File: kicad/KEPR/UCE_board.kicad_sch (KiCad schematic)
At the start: 12 parts, among them IC1 ACS37041KLHBLT-010B3, IC2 ACS37041KLHBLT-010B3, IC3 ACS37041KLHBLT-010B3, U1 REF193, U2 STM32G484CETx, U3 AMS1117-3.3

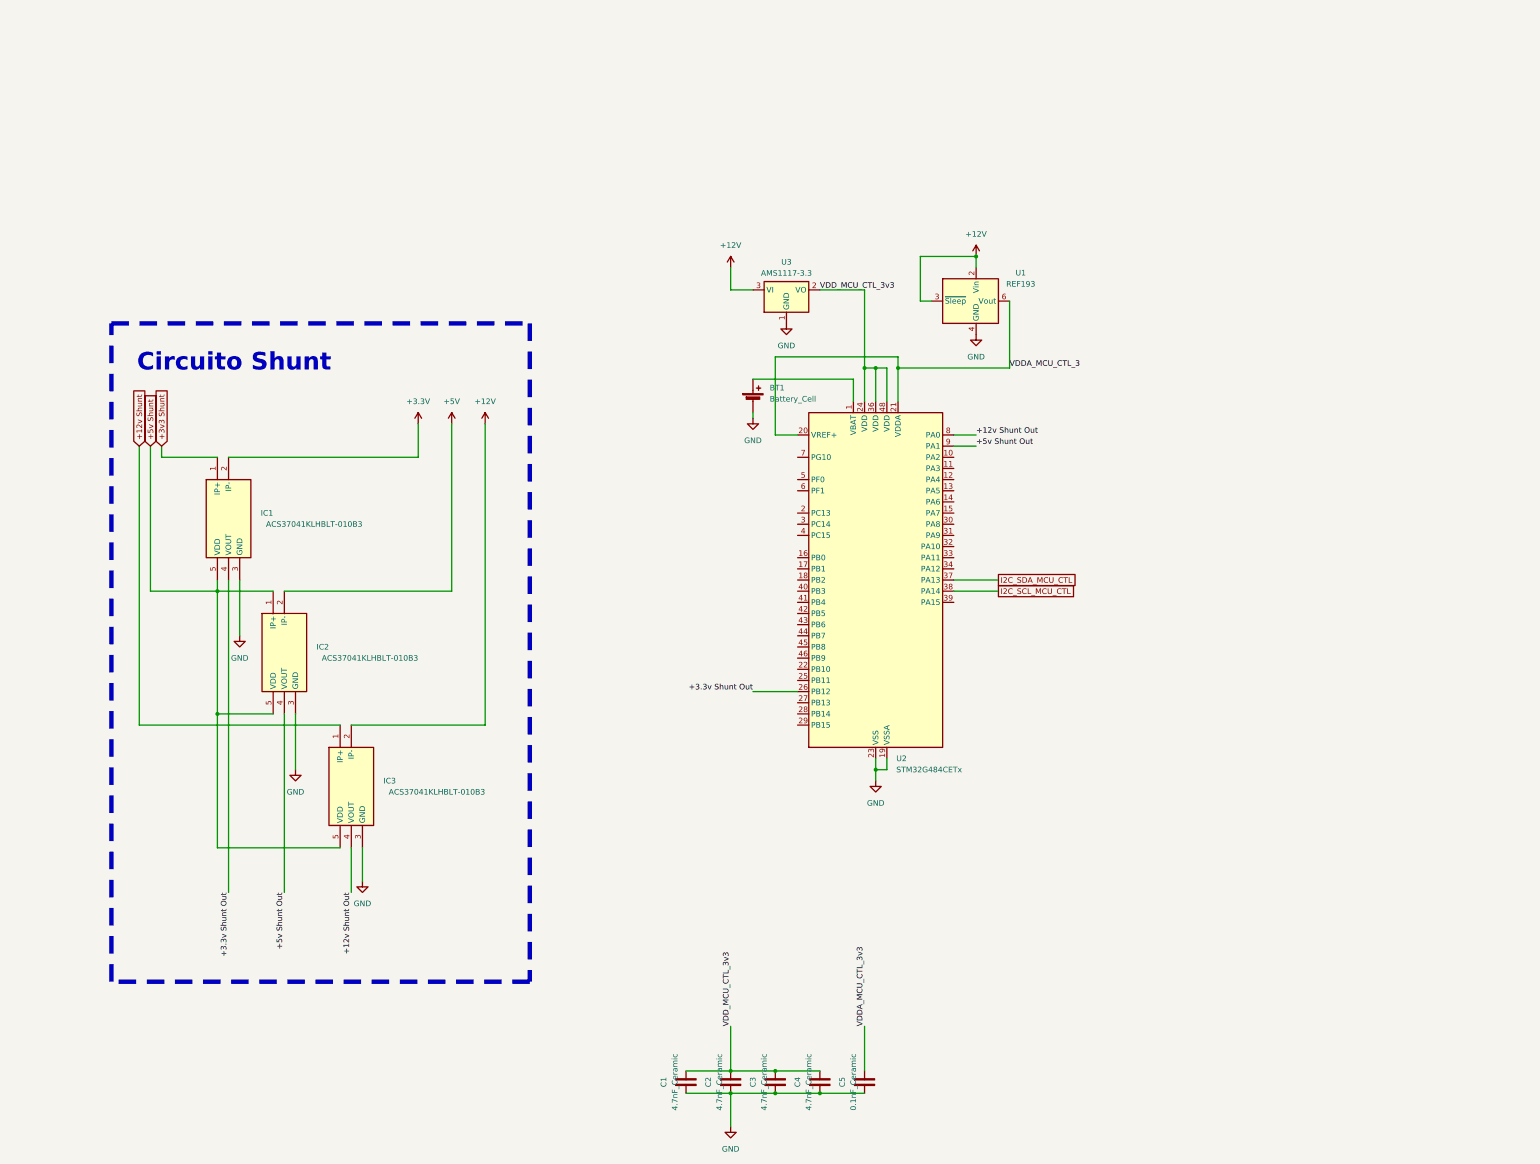
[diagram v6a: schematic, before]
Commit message: Adicionado o display oled e mais trilhas.
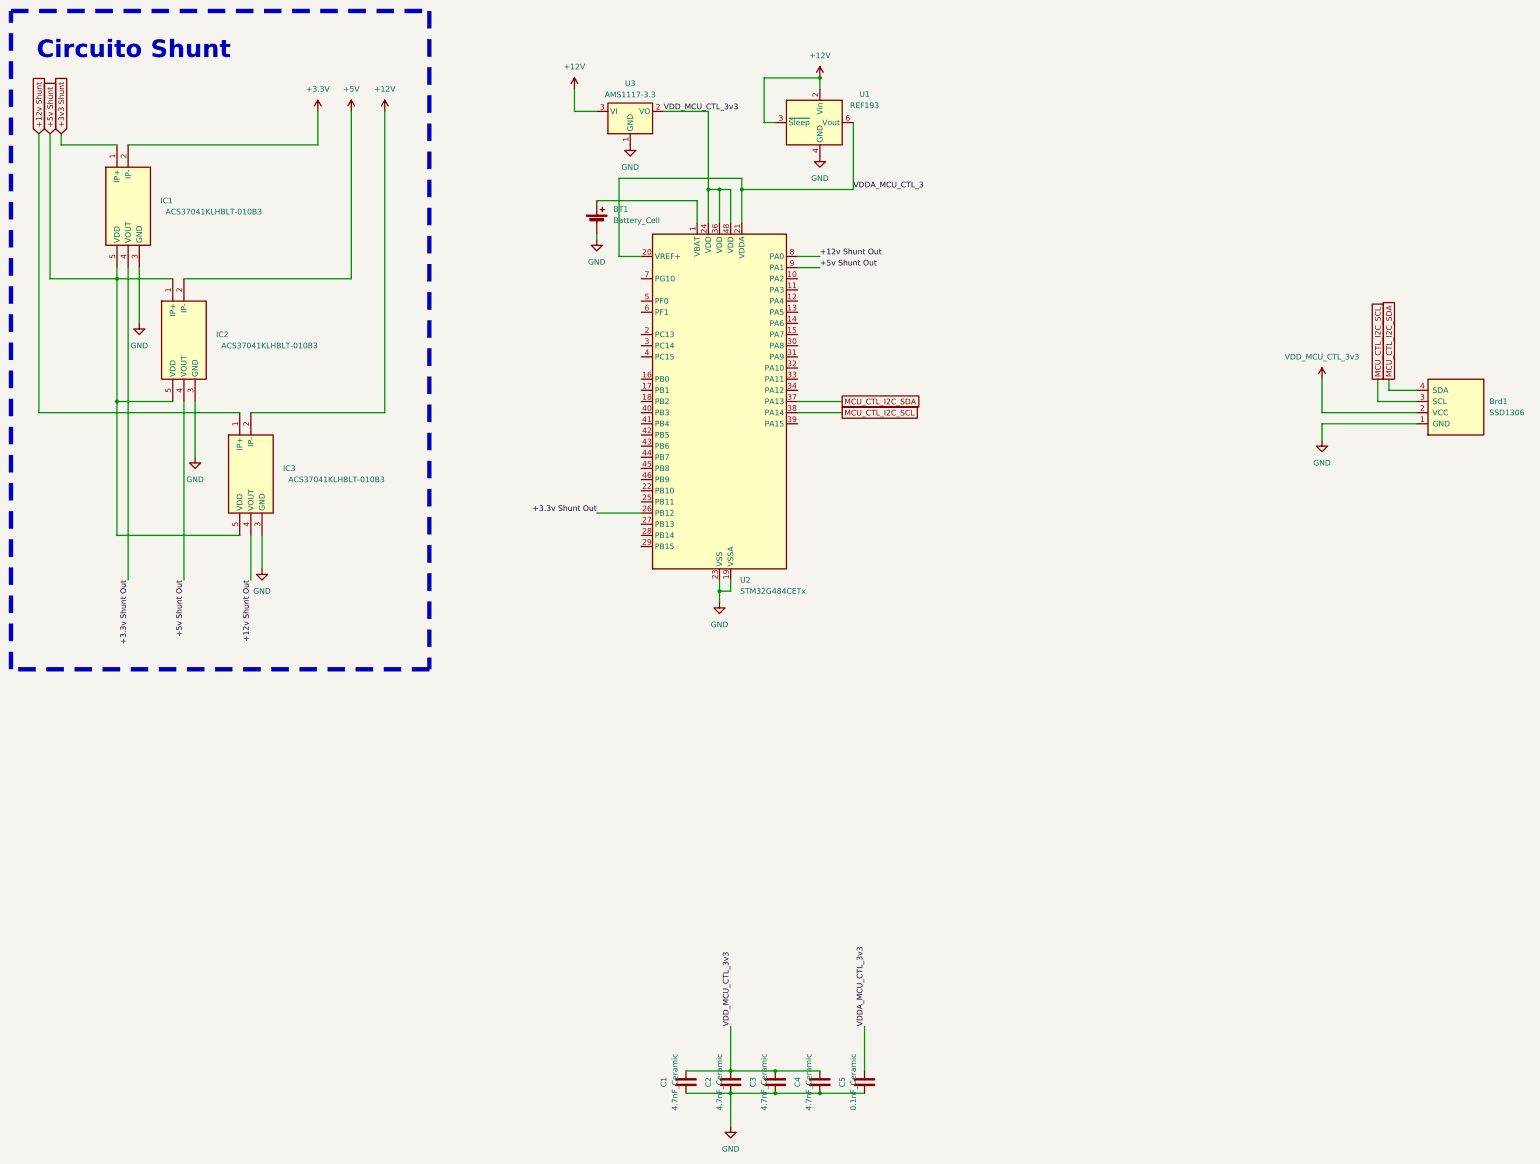
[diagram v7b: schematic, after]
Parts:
- added Brd1: SSD1306, SSD1306:128x64OLED, symbol SSD1306-128x64_OLED:SSD1306
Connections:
- net GND: now also Brd1.1 (GND)
- net VDD_MCU_CTL_3v3: now also Brd1.2 (VCC)
- net I2C_SCL_MCU_CTL renamed MCU_CTL_I2C_SCL
- net MCU_CTL_I2C_SCL: now also Brd1.3 (SCL)
- net I2C_SDA_MCU_CTL renamed MCU_CTL_I2C_SDA
- net MCU_CTL_I2C_SDA: now also Brd1.4 (SDA)
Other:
- moved on the sheet: BT1, IC1, IC2, IC3, U1, U2, U3

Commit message: mais ajustes de trilha.
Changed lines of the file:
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@@
+		)
+	)
+	(label "VDD_MCU_CTL_3v3"
+		(at 323.85 54.61 0)
+		(effects
+			(font
+				(size 1.27 1.27)
+			)
+			(justify left bottom)
 		)
 	)
@@
 		)
 	)
+	(global_label "MCU_CTL_I2C_SCL"
+		(shape passive)
+		(at 328.93 29.21 0)
+		(fields_autoplaced yes)
+		(effects
+			(font
+				(size 1.27 1.27)
+			)
+			(justify left)
+		)
+		(property "Intersheetrefs" "${INTERSHEET_REFS}"
+			(at 347.6162 29.21 0)
+			(effects
+				(font
+					(size 1.27 1.27)
+				)
+				(justify left)
+				(hide yes)
+			)
+		)
+	)
 	(global_label "+12v Shunt"
 		(shape input)
@@
 			)
 		)
+	)
+	(global_label "MCU_CTL_I2C_SDA"
+		(shape passive)
+		(at 328.93 31.75 0)
+		(fields_autoplaced yes)
+		(effects
+			(font
+				(size 1.27 1.27)
+			)
+			(justify left)
+		)
+		(property "Intersheetrefs" "${INTERSHEET_REFS}"
+			(at 347.6767 31.75 0)
+			(effects
+				(font
+					(size 1.27 1.27)
+				)
+				(justify left)
+				(hide yes)
+			)
+		)
+	)
+	(rule_area
+		(polyline
+			(pts
+				(xy 350.52 25.4) (xy 350.52 38.1) (xy 345.44 38.1) (xy 317.5 38.1) (xy 317.5 25.4) (xy 317.5 25.4)
+			)
+			(stroke
+				(width 0)
+				(type dash)
+			)
+			(fill
+				(type none)
+			)
+		)
+	)
+	(rule_area
+		(polyline
+			(pts
+				(xy 317.5 49.53) (xy 350.52 49.53) (xy 350.52 63.5) (xy 317.5 63.5)
+			)
+			(stroke
+				(width 0)
+				(type dash)
+			)
+			(fill
+				(type none)
+			)
+		)
+	)
+	(netclass_flag ""
+		(length 2.54)
+		(shape round)
+		(at 326.39 49.53 0)
+		(fields_autoplaced yes)
+		(effects
+			(font
+				(size 1.27 1.27)
+			)
+			(justify left bottom)
+		)
+		(property "Netclass" "VDD_MCU_CTL"
+			(at 327.0885 46.99 0)
+			(effects
+				(font
+					(size 1.27 1.27)
+				)
+				(justify left)
+			)
+		)
+		(property "Component Class" ""
+			(at -87.63 -8.89 0)
+			(effects
+				(font
+					(size 1.27 1.27)
+					(italic yes)
+				)
+			)
+		)
+	)
+	(netclass_flag ""
+		(length 2.54)
+		(shape round)
+		(at 331.47 25.4 0)
+		(fields_autoplaced yes)
+		(effects
+			(font
+				(size 1.27 1.27)
+			)
+			(justify left bottom)
+		)
+		(property "Netclass" "I2C"
+			(at 332.1685 22.86 0)
+			(effects
+				(font
+					(size 1.27 1.27)
+				)
+				(justify left)
+			)
+		)
+		(property "Component Class" ""
+			(at -113.03 -27.94 0)
+			(effects
+				(font
+					(size 1.27 1.27)
+					(italic yes)
+				)
+			)
+		)
